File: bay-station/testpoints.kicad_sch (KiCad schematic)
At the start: 14 parts

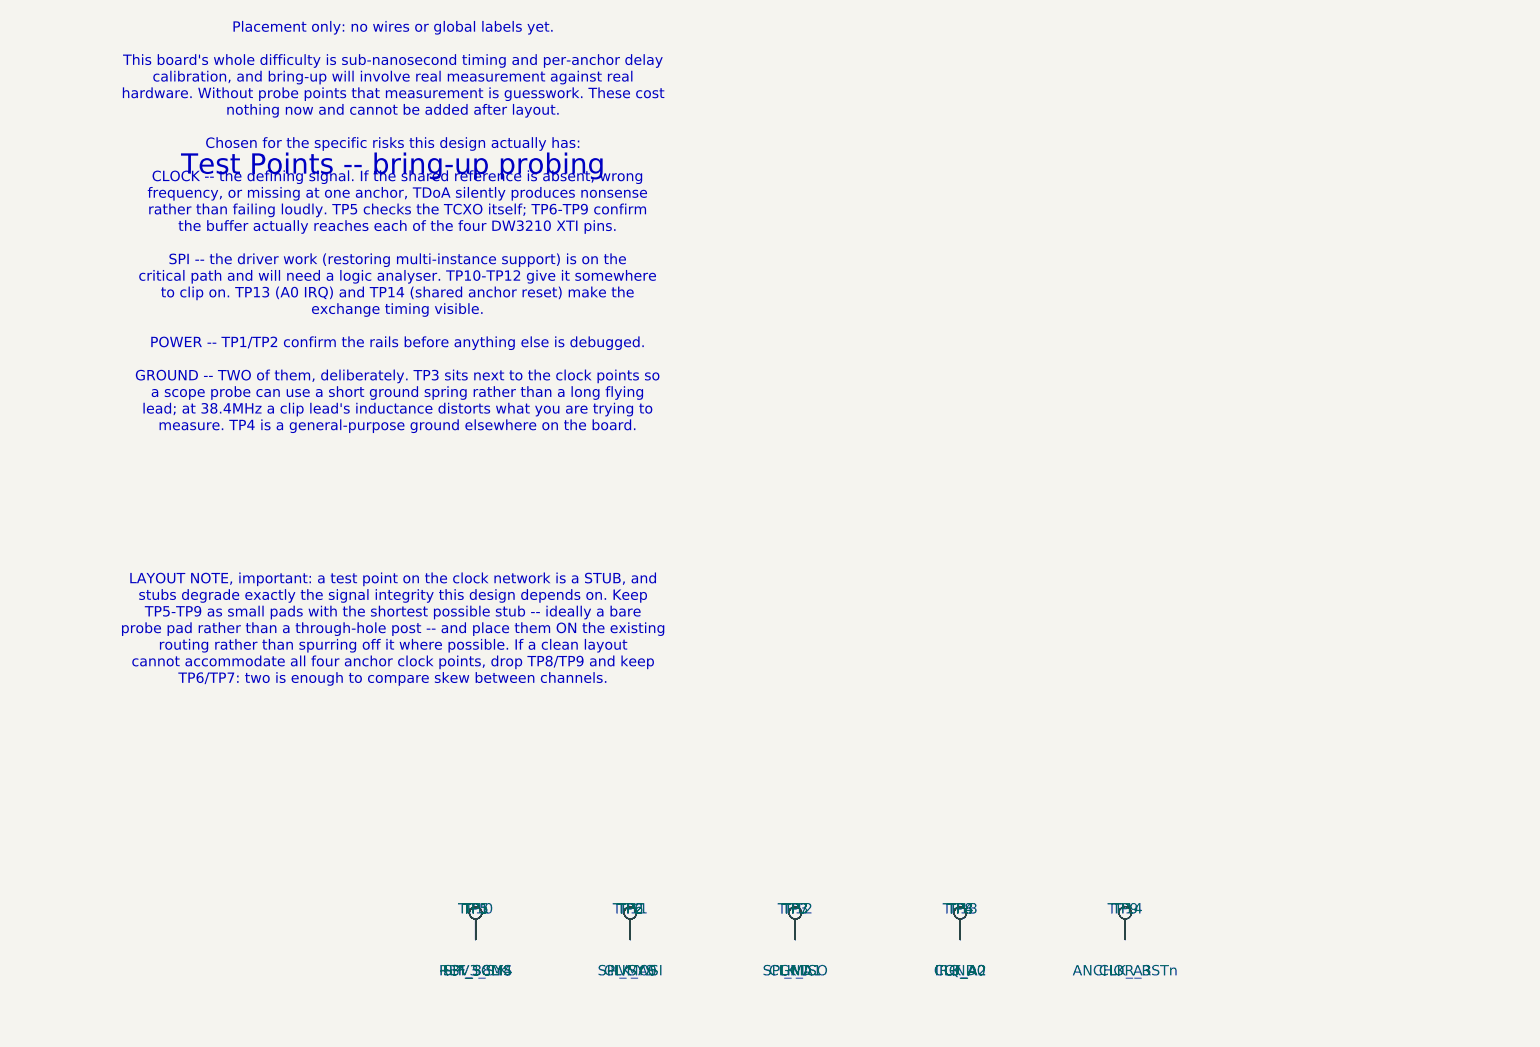
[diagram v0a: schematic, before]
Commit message: Wire up power_bms, regulation and programming_debug; tie off floating grounds
The bay station was built entirely from global labels and power symbols --
zero drawn wires on any sheet. This starts converting the power path to
explicit wiring and connects the grounds that were left floating:

- power_bms: 62 wires; 31 label justifications flipped left->right where
  the labels were mirrored. No symbols added or removed.
- regulation: 11 wires, 3 junctions, 5 GND symbols (#PWR01-05).
- programming_debug: 2 wires, 1 junction, 1 GND symbol (#PWR06).

ERC goes 518 -> 497 violations (494 -> 473 errors), entirely in
pin_not_connected (360 -> 342), power_pin_not_driven (98 -> 96) and
pin_not_driven (36 -> 35). Nothing regressed. The remaining 342
pin_not_connected are the sheets that are still label-only.

Unavoidable churn in this commit: KiCad 10 re-serialized seven sheets from
8.0 format (version 20231120) to 10.0 (20260306) on save -- clock_dist,
connectivity, gnss, indicators, programming_debug, testpoints, uwb_array.
That accounts for most of the diff; those seven have no content change
beyond it. CLAUDE.md asks that the format not be bumped as a side effect,
but it cannot be split out here: kicad-cli sch upgrade serializes
differently from the GUI and leaves ~3700 lines of residual churn, so a
format-only commit would be tidier in shape and no more honest. Four
sheets were already on 10.0 format before this commit.

Co-Authored-By: Claude Opus 5 (1M context) <noreply@anthropic.com>
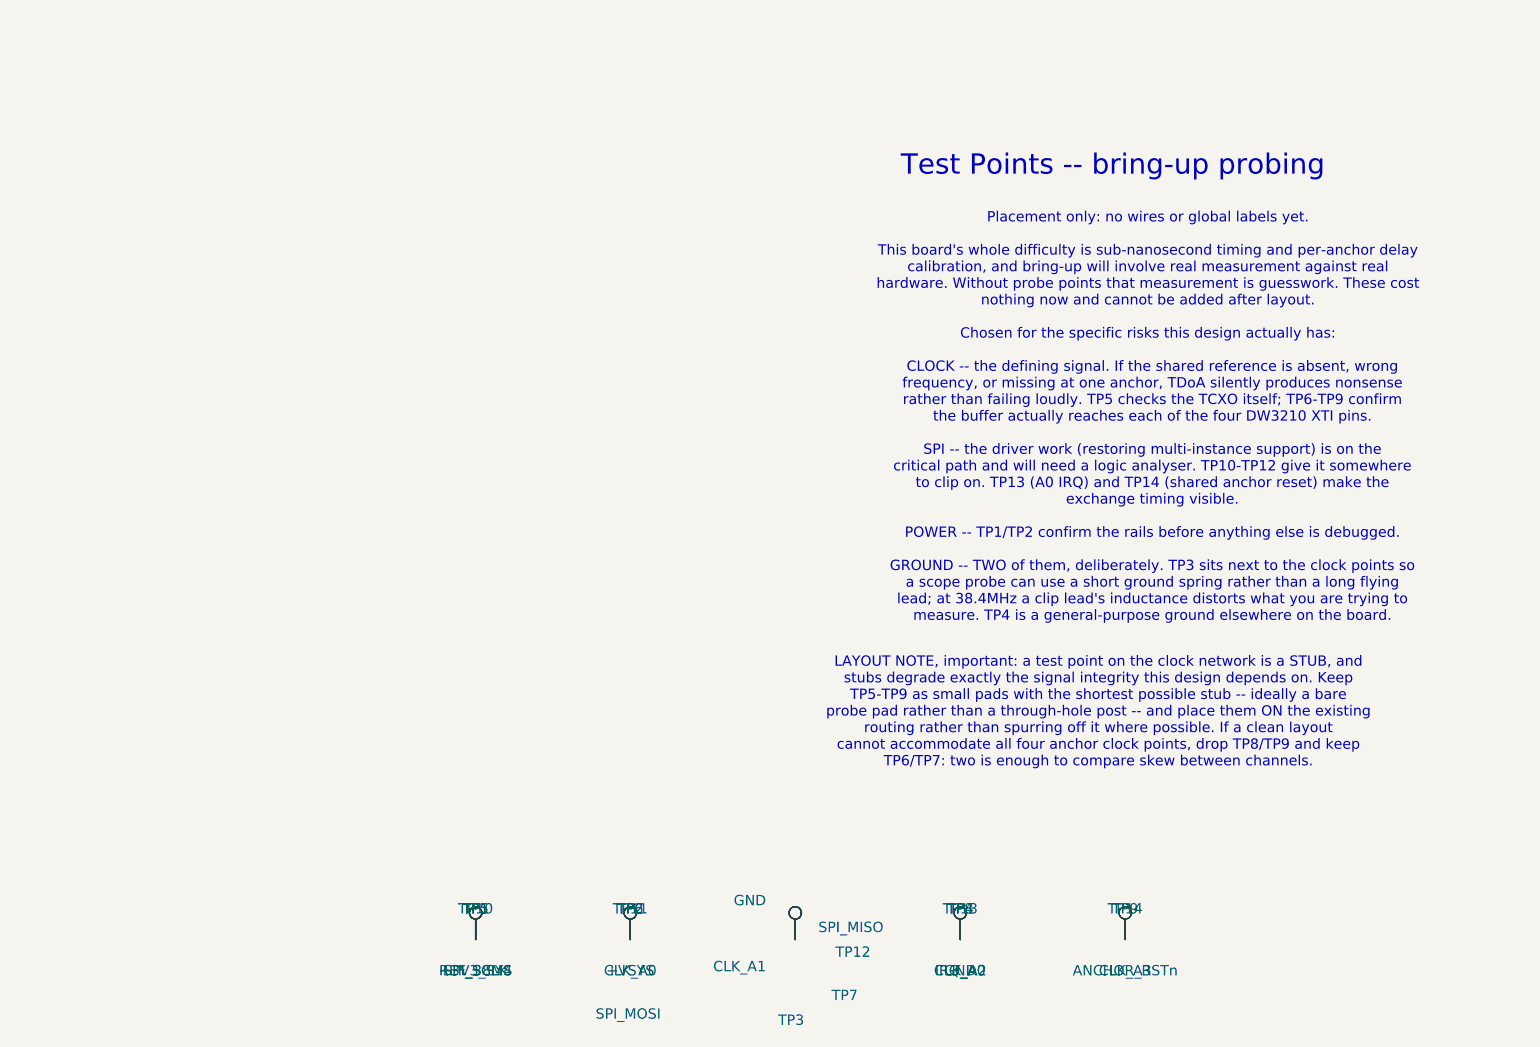
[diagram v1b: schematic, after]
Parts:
- removed TP1: +3V3_SYS, TestPoint:TestPoint_Pad_D1.5mm, symbol Connector:TestPoint
- removed TP2: +VSYS, TestPoint:TestPoint_Pad_D1.5mm, symbol Connector:TestPoint
- removed TP3: GND, TestPoint:TestPoint_Pad_D1.5mm, symbol Connector:TestPoint
- added TP7: CLK_A1, TestPoint:TestPoint_Pad_D1.5mm, symbol Connector:TestPoint
- added TP8: CLK_A2, TestPoint:TestPoint_Pad_D1.5mm, symbol Connector:TestPoint
- added TP9: CLK_A3, TestPoint:TestPoint_Pad_D1.5mm, symbol Connector:TestPoint
- TP1: renamed from TP4; value GND -> +3V3_SYS
- TP2: renamed from TP5; value REF_38M4 -> +VSYS
- TP3: renamed from TP6; value CLK_A0 -> GND
- TP4: renamed from TP7; value CLK_A1 -> GND
- TP5: renamed from TP8; value CLK_A2 -> REF_38M4
- TP6: renamed from TP9; value CLK_A3 -> CLK_A0
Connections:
- net at TP10.1: now also TP1.1, TP5.1; no longer TP2.1
- net at TP11.1: now also TP2.1, TP6.1; no longer TP3.1
- net at TP12.1: now also TP3.1, TP7.1; no longer TP4.1
- net at TP14.1: now also TP9.1; no longer TP6.1
- new net: TP13.1, TP4.1, TP8.1
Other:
- moved on the sheet: TP1, TP2, TP3, TP4, TP5, TP6
